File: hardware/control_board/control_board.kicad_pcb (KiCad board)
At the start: 2 copper layers, 50 x 40 mm, 7 parts, among them J1 USB-C, J2 USB-C, U1 STUSB4500QTR

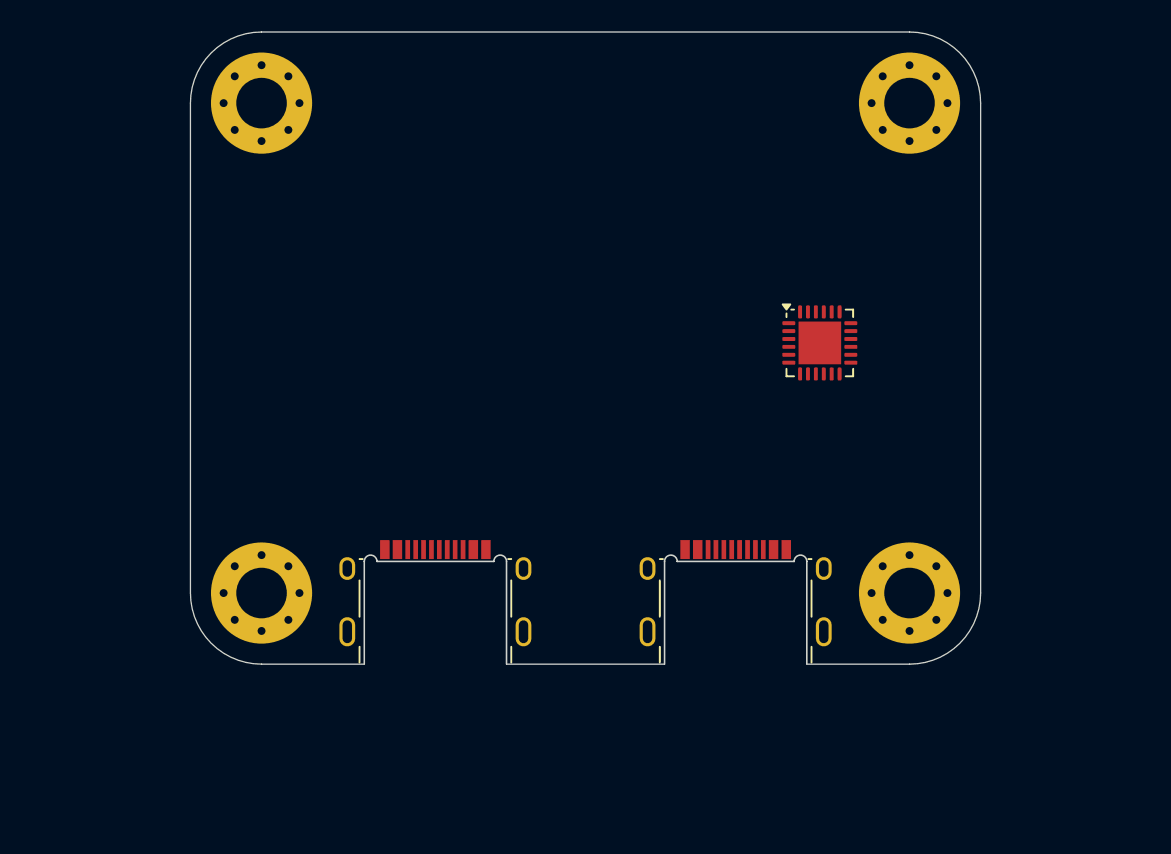
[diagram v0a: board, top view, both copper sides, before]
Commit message: added connectors
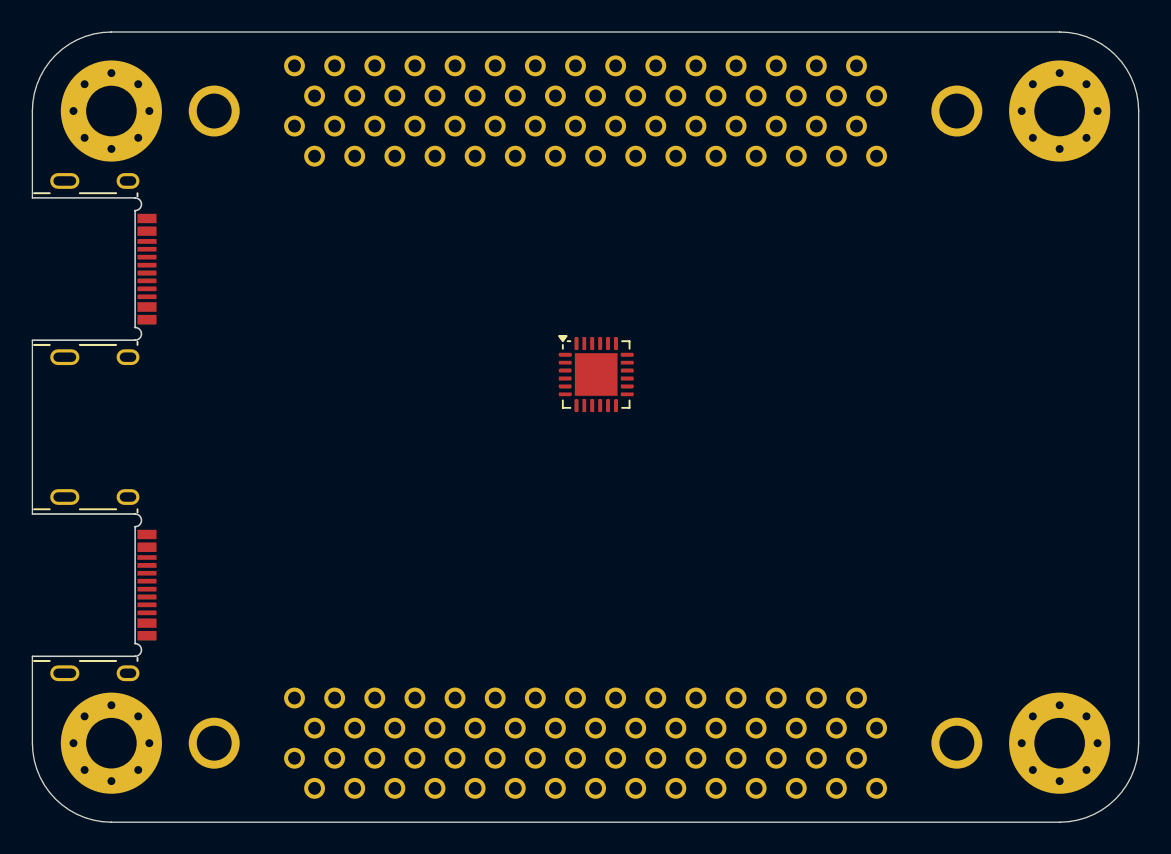
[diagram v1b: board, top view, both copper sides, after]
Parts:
- added J3: TX24-60R-6ST-H1E, Library:JAE_TX24-60R-6ST-H1E, B.Cu at (135.0, 85.0)
- added J4: TX24-60R-6ST-H1E, Library:JAE_TX24-60R-6ST-H1E, B.Cu at (135.0, 125.0)
- moved J2 41.3 mm to (103.2, 115.0), turned to -90 degrees
- moved J1 31.2 mm to (103.2, 95.0), turned to -90 degrees
- moved U1 14.3 mm to (135.7, 101.7)
- moved H3 13.4 mm to (165.0, 125.0)
- moved H4 13.4 mm to (105.0, 125.0)
- moved H1 9.51 mm to (105.0, 85.0)
- moved H2 9.51 mm to (165.0, 85.0)
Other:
- board size 50 x 40 mm -> 70 x 50 mm
- copper layers 2 -> 4
